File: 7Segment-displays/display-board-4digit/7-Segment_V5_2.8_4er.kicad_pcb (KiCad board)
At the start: 2 copper layers, 51 x 12 mm, 6 parts, among them J1 Conn_02x08_Odd_Even, U1 HDSM-443B_CC_2Digit_7Segment_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, U2 HDSM-443B_CC_2Digit_7Segment_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

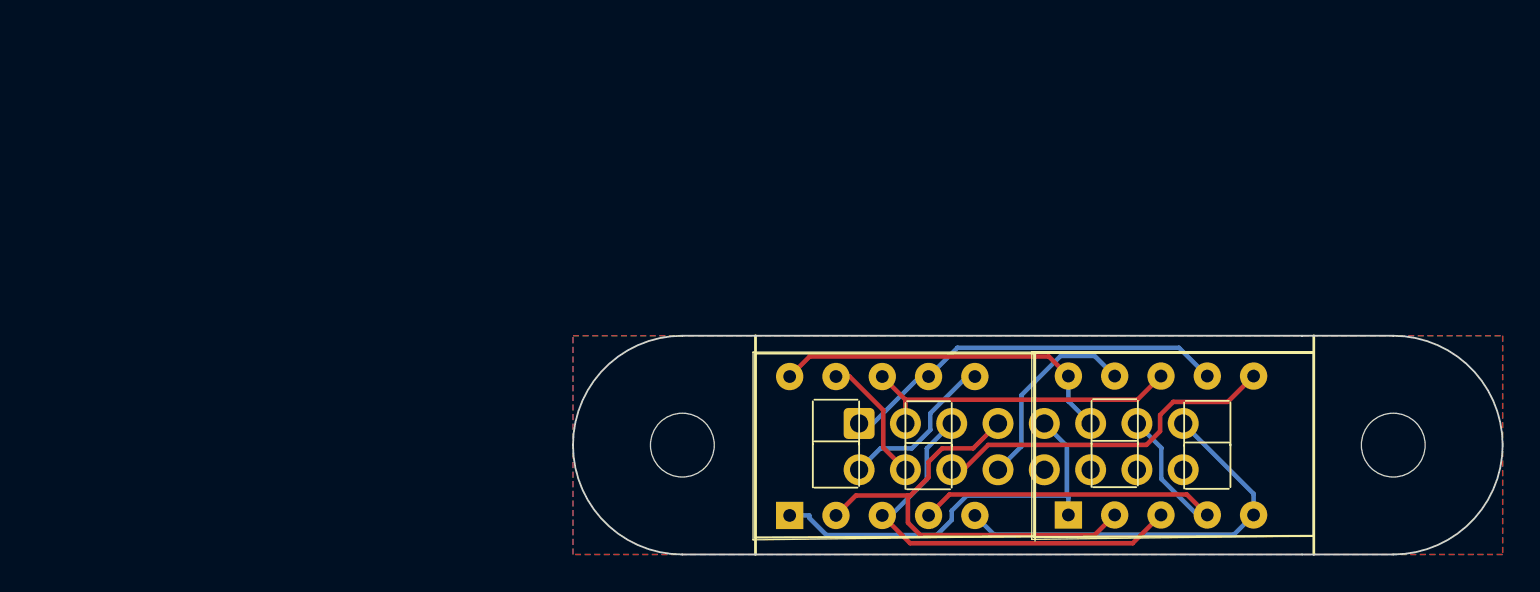
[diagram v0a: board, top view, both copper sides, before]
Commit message: new symbol and footprint, connector rotated by 180 degree, new routing
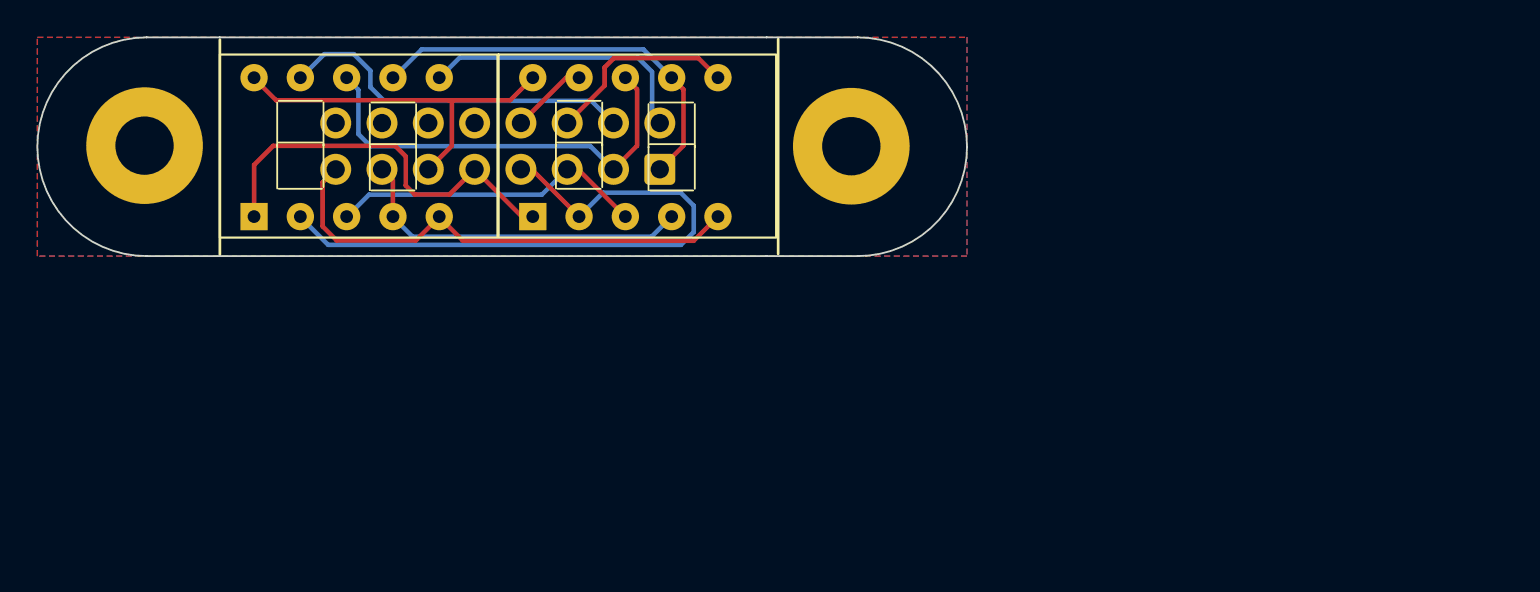
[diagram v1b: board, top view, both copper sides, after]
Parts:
- removed G3: LOGO, Logo:MobiFlight1
- removed REF1, REF2: MountingHole_3.5mm, MountingHole:MountingHole_3.5mm
- added H1: MountingHole 3.2mm, MountingHole:MountingHole_3.2mm_M3_Pad, F.Cu at (76.5, 59.6)
- added H2: MountingHole 3.2mm, MountingHole:MountingHole_3.2mm_M3_Pad, F.Cu at (115.3, 59.6)
- U1, U2: footprint Display_7Segment:STH_7_2 Digits_0.28_CC -> MobiFlight:STH_7_2 Digits_0.28_CC
- moved U2 33.6 mm to (89.6, 60.4)
- moved U1 33.6 mm to (104.9, 60.4)
- moved J1 17.7 mm to (104.8, 60.9), turned to 90 degrees
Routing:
- net /DIG1: track 7.13 -> 19.8 mm
- net /D: track 25.0 -> 35.3 mm
- net /DIG2: track 19.2 -> 10.8 mm
- net /DIG0: track 9.00 -> 15.9 mm
- net /DIG3: track 11.1 -> 4.22 mm
- net /B: track 17.7 -> 24.0 mm
- net /C: track 23.5 -> 18.5 mm
- net /DP: track 22.8 -> 27.1 mm
- net /G: track 23.2 -> 19.6 mm
- net /A: track 21.5 -> 22.9 mm
- net /F: track 19.3 -> 20.7 mm
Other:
- board text added: "MobiFlight Display System 2.8mm ${REVISION}"
- board text added: "MobiFlight.com/7smb"
- board text removed: "MobiFlight Display System 2.8mm V5.1"
